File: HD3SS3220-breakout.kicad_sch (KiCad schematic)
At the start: 36 parts, among them J2 USB_C_Receptacle, SW2 SW_DIP_x04, U4 HD3SS3220RNHR, U5 U-A-39SS-Y-1, U6 HT7533-1_C14289, U7 TPD4EUSB30, U8 TPD2EUSB30, U9 PZ254-2-08-WS

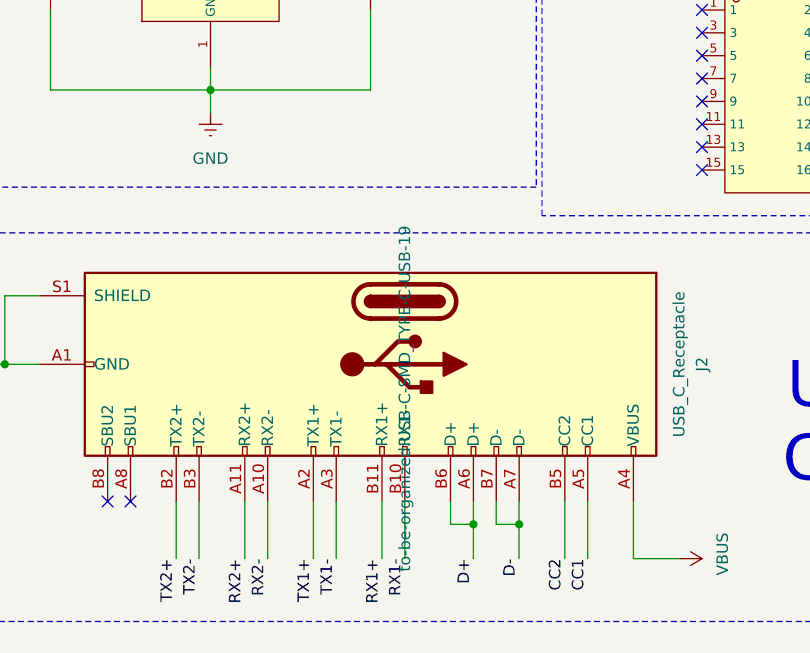
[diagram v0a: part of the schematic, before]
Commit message: Added dip switch footprint to library and PCB editor
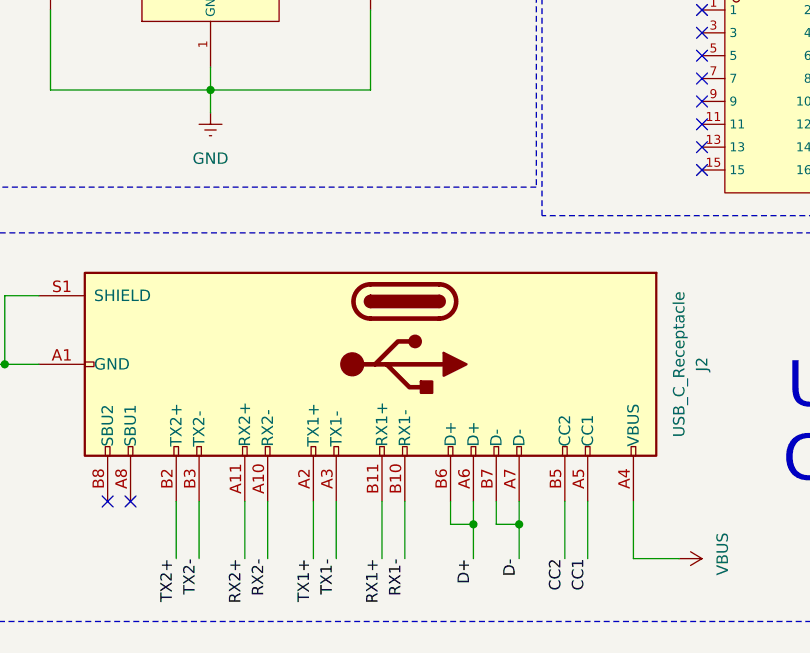
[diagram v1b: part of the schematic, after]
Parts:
- SW2: footprint (none) -> Button_Switch_SMD:SW4
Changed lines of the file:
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@@
 		(property "Footprint" "to-be-organized:USB-C-SMD_TYPE-C-USB-19"
 			(at 68.58 171.45 0)
+			(hide yes)
 			(show_name no)
 			(do_not_autoplace no)
@@
 			)
 		)
-		(property "Footprint" ""
+		(property "Footprint" "Button_Switch_SMD:SW4"
 			(at 204.47 146.05 0)
 			(hide yes)

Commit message: added more footprints
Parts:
- C1, C11, C12, C2, C3, C4, C5, C6: footprint (none) -> Capacitor_SMD:C_0603_1608Metric
- DIR_LED1, VBUS_LED1: footprint (none) -> LED_SMD:LED_0603_1608Metric
- R10, R6, R7, R8, R9: footprint (none) -> Resistor_SMD:R_0603_1608Metric
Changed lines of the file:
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@@
 (kicad_sch
-	(version 20260306)
+	(version 20260101)
 	(generator "eeschema")
 	(generator_version "10.0")
@@
 			)
 		)
-		(property "Footprint" ""
+		(property "Footprint" "Resistor_SMD:R_0603_1608Metric"
 			(at 175.26 49.53 0)
 			(hide yes)
@@
 			)
 		)
-		(property "Footprint" ""
+		(property "Footprint" "Capacitor_SMD:C_0603_1608Metric"
 			(at 247.65 52.07 0)
 			(hide yes)
@@
 			)
 		)
-		(property "Footprint" ""
+		(property "Footprint" "LED_SMD:LED_0603_1608Metric"
 			(at 154.94 92.71 0)
 			(hide yes)
@@
 			)
 		)
-		(property "Footprint" ""
+		(property "Footprint" "Resistor_SMD:R_0603_1608Metric"
 			(at 189.23 143.51 0)
 			(hide yes)
@@
 			)
 		)
-		(property "Footprint" ""
+		(property "Footprint" "Capacitor_SMD:C_0603_1608Metric"
 			(at 255.27 67.31 0)
 			(hide yes)
@@
 			)
 		)
-		(property "Footprint" ""
+		(property "Footprint" "Resistor_SMD:R_0603_1608Metric"
 			(at 217.17 146.05 0)
 			(hide yes)
@@
 			)
 		)
-		(property "Footprint" ""
+		(property "Footprint" "Resistor_SMD:R_0603_1608Metric"
 			(at 217.17 148.59 0)
 			(hide yes)
@@
 			)
 		)
-		(property "Footprint" ""
+		(property "Footprint" "Capacitor_SMD:C_0603_1608Metric"
 			(at 247.65 64.77 0)
 			(hide yes)
@@
 			)
 		)
-		(property "Footprint" ""
+		(property "Footprint" "Capacitor_SMD:C_0603_1608Metric"
 			(at 64.77 125.73 0)
 			(hide yes)
@@
 			)
 		)
-		(property "Footprint" ""
+		(property "Footprint" "LED_SMD:LED_0603_1608Metric"
 			(at 144.78 92.71 0)
 			(hide yes)
@@
 			)
 		)
-		(property "Footprint" ""
+		(property "Footprint" "Capacitor_SMD:C_0603_1608Metric"
 			(at 171.45 77.47 0)
 			(hide yes)
@@
 			)
 		)
-		(property "Footprint" ""
+		(property "Footprint" "Capacitor_SMD:C_0603_1608Metric"
 			(at 29.21 125.73 0)
 			(hide yes)
@@
 			)
 		)
-		(property "Footprint" ""
+		(property "Footprint" "Resistor_SMD:R_0603_1608Metric"
 			(at 166.37 41.91 0)
 			(hide yes)
@@
 			)
 		)
-		(property "Footprint" ""
+		(property "Footprint" "Capacitor_SMD:C_0603_1608Metric"
 			(at 176.53 80.01 0)
 			(hide yes)
@@
 			)
 		)
-		(property "Footprint" ""
+		(property "Footprint" "Capacitor_SMD:C_0603_1608Metric"
 			(at 255.27 54.61 0)
 			(hide yes)

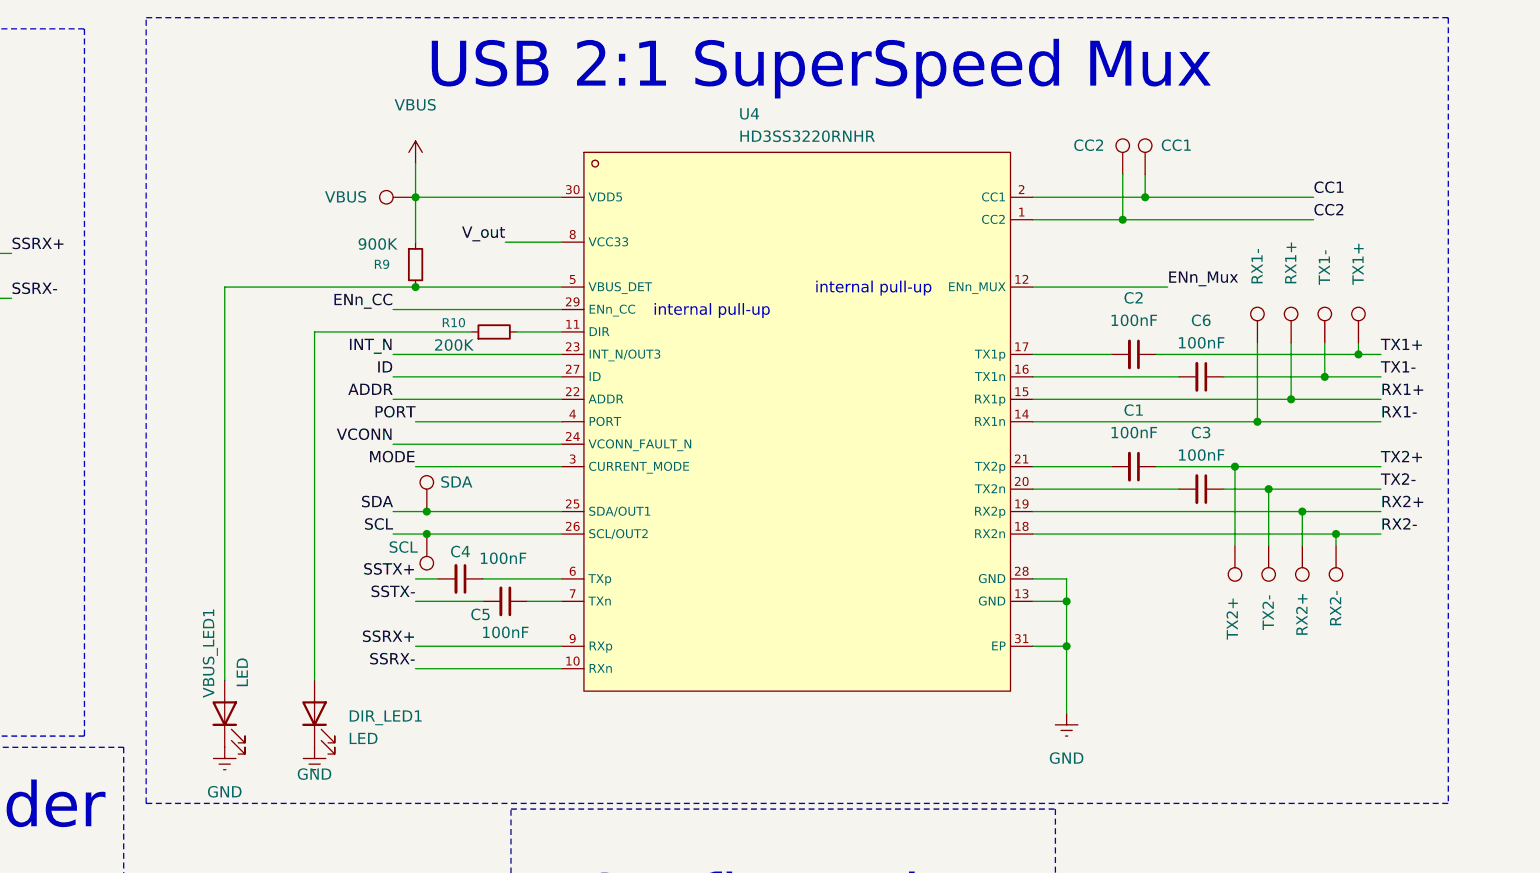
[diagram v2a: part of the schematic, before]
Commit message: Fixed mux footprint somewhat, starting to route
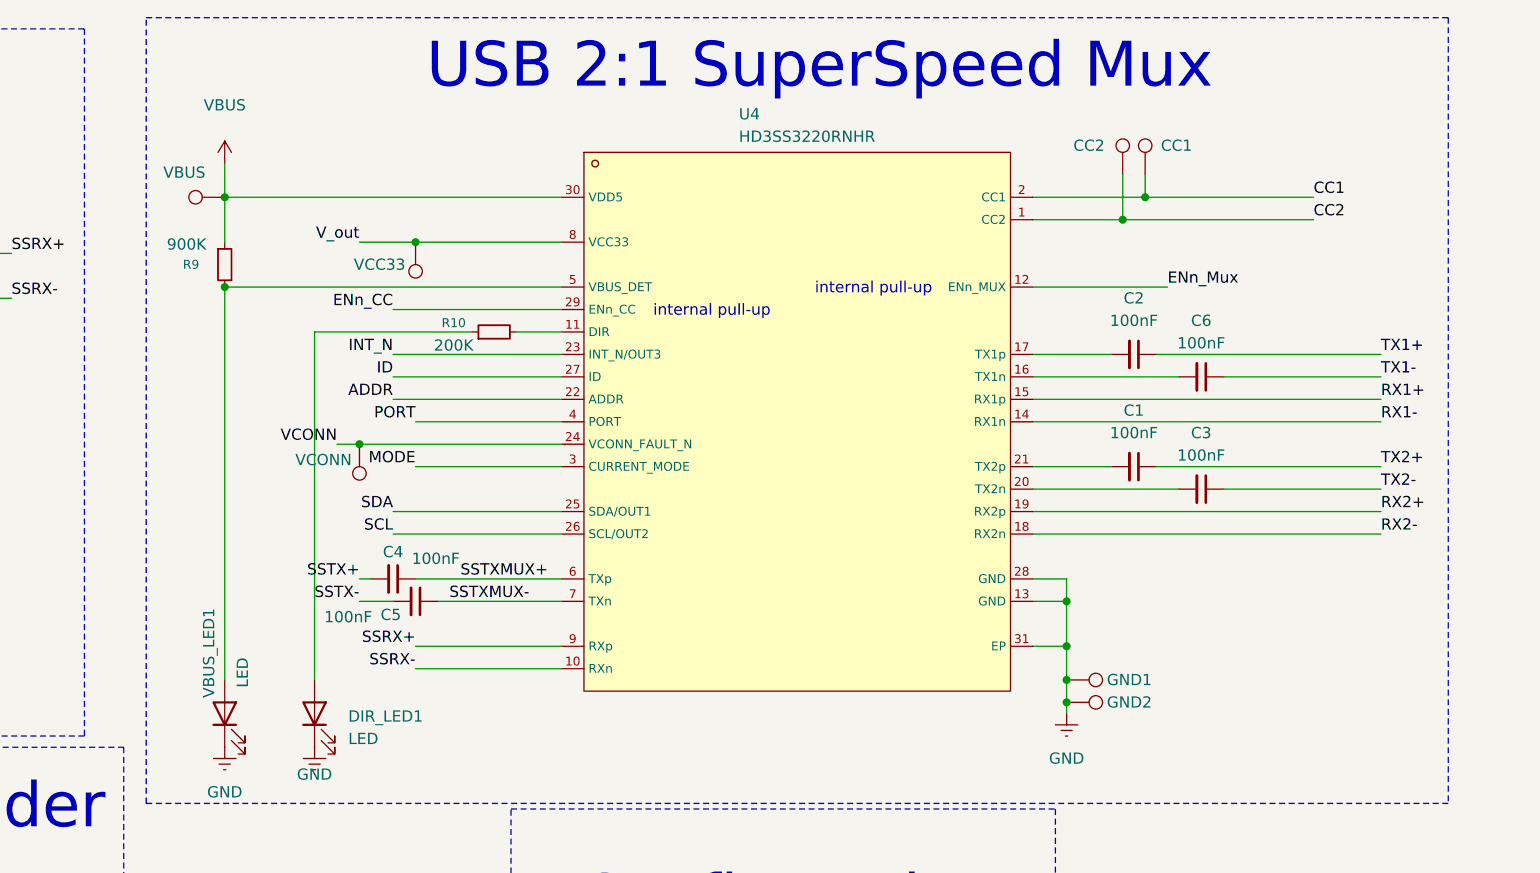
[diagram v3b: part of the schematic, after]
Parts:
- removed TP1: RX2-, symbol Connector:TestPoint
- removed TP2: RX1-, symbol Connector:TestPoint
- removed TP3: RX2+, symbol Connector:TestPoint
- removed TP4: TX2-, symbol Connector:TestPoint
- removed TP5: TX2+, symbol Connector:TestPoint
- removed TP6: RX1+, symbol Connector:TestPoint
- removed TP7: TX1-, symbol Connector:TestPoint
- removed TP8: TX1+, symbol Connector:TestPoint
- added TP14: GND1, TestPoint:TestPoint_Keystone_5000-5004_Miniature, symbol Connector:TestPoint
- added TP15: GND2, TestPoint:TestPoint_Keystone_5000-5004_Miniature, symbol Connector:TestPoint
- TP10, TP11, TP9: footprint (none) -> TestPoint:TestPoint_Pad_D1.5mm
- TP12: value SDA -> VCC33; footprint (none) -> TestPoint:TestPoint_Pad_D1.5mm
- TP13: value SCL -> VCONN; footprint (none) -> TestPoint:TestPoint_Pad_D1.5mm
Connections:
- net GND: now also TP14.1, TP15.1
- net SCL: no longer TP13.1
- net SDA: no longer TP12.1
- net VCONN: now also TP13.1
- net V_out: now also TP12.1
- net SSTXMUX+: now reaches C4.1, U4.6 (TXp)
- net SSTXMUX-: now reaches C5.1, U4.7 (TXn)
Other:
- moved on the sheet: C4, C5, R9

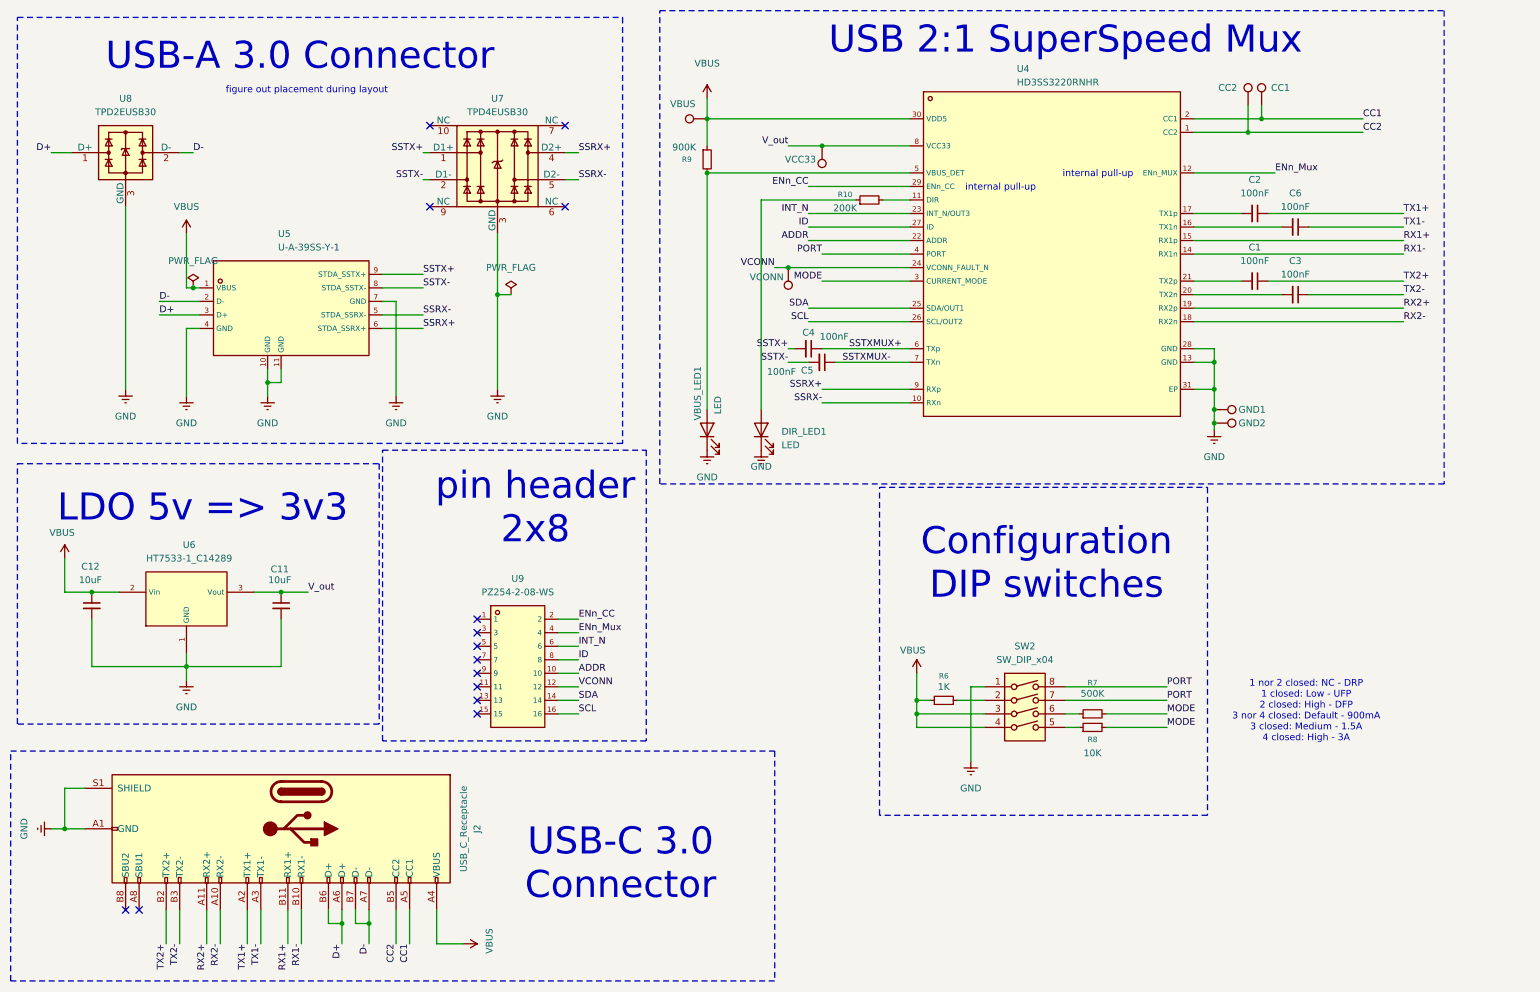
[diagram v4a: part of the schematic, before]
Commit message: Hierarchy Schematic Implementation and Clean-up (Please Refer to this Version for previous sym-lib-table)
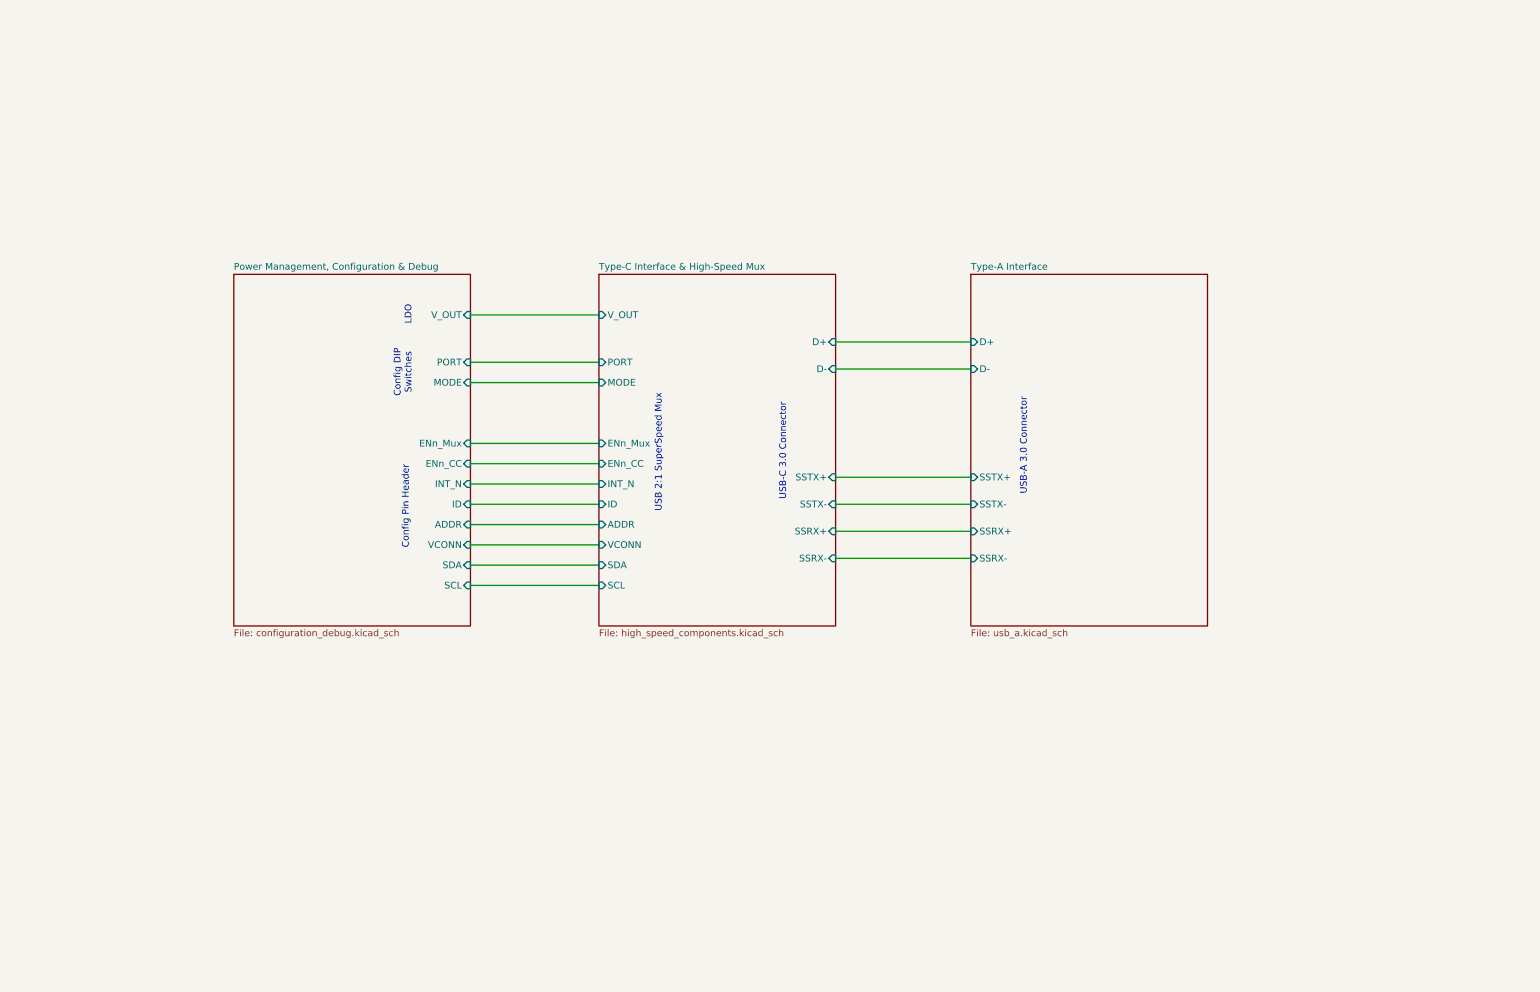
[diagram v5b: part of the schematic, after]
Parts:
- removed C1, C2, C3, C4, C5, C6: 100nF, Capacitor_SMD:C_0603_1608Metric, symbol Device:C_Small
- removed C11, C12: 10uF, Capacitor_SMD:C_0603_1608Metric, symbol Device:C_Small
- removed DIR_LED1, VBUS_LED1: LED, LED_SMD:LED_0603_1608Metric, symbol Device:LED
- removed J2: USB_C_Receptacle, to-be-organized:USB-C-SMD_TYPE-C-USB-19, symbol Connector:USB_C_Receptacle
- removed R10: 200K, Resistor_SMD:R_0603_1608Metric, symbol Device:R_Small
- removed R6: 1K, Resistor_SMD:R_0603_1608Metric, symbol Device:R_Small
- removed R7: 500K, Resistor_SMD:R_0603_1608Metric, symbol Device:R_Small
- removed R8: 10K, Resistor_SMD:R_0603_1608Metric, symbol Device:R_Small
- removed R9: 900K, Resistor_SMD:R_0603_1608Metric, symbol Device:R_Small
- removed SW2: SW_DIP_x04, Button_Switch_SMD:SW4, symbol Switch:SW_DIP_x04
- removed TP10: CC2, TestPoint:TestPoint_Pad_D1.5mm, symbol Connector:TestPoint
- removed TP11: VBUS, TestPoint:TestPoint_Pad_D1.5mm, symbol Connector:TestPoint
- removed TP12: VCC33, TestPoint:TestPoint_Pad_D1.5mm, symbol Connector:TestPoint
- removed TP13: VCONN, TestPoint:TestPoint_Pad_D1.5mm, symbol Connector:TestPoint
- removed TP14: GND1, TestPoint:TestPoint_Keystone_5000-5004_Miniature, symbol Connector:TestPoint
- removed TP15: GND2, TestPoint:TestPoint_Keystone_5000-5004_Miniature, symbol Connector:TestPoint
- removed TP9: CC1, TestPoint:TestPoint_Pad_D1.5mm, symbol Connector:TestPoint
- removed U4: HD3SS3220RNHR, Interface_USB:HD3SS3220IRNHR, symbol Interface_USB:HD3SS3220RNHR
- removed U5: U-A-39SS-Y-1, footprint:USB-3.0-A_U-A-39SS-Y-1, symbol Connector_USB-custom:U-A-39SS-Y-1
- removed U6: HT7533-1_C14289, footprint:SOT-89-3_L4.5-W2.5-P1.50-LS4.2-BR, symbol Regulator_Linear:HT7533-1_C14289
- removed U7: TPD4EUSB30, Package_SON:USON-10_2.5x1.0mm_P0.5mm, symbol Power_Protection:TPD4EUSB30
- removed U8: TPD2EUSB30, Package_TO_SOT_SMD:Texas_DRT-3, symbol Power_Protection:TPD2EUSB30
- removed U9: PZ254-2-08-WS, footprint:HDR-SMD_16P-P2.54-H-M-R2-C8-W12.0-N, symbol PZ254-2-08-WS:PZ254-2-08-WS
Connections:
- no-connect marks 14 -> 0
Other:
- added sheet Power Management, Configuration & Debug (configuration_debug.kicad_sch)
- added sheet Type-A Interface (usb_a.kicad_sch)
- added sheet Type-C Interface & High-Speed Mux (high_speed_components.kicad_sch)
- note added: "Config DIP Switches"
- note added: "Config Pin Header"
- note added: "LDO"
- note removed: "1 nor 2 closed: NC - DRP 1 closed: Low - UFP 2 closed: High - DFP 3 nor 4 closed: Default - 900mA 3 closed: Medium - 1.5A 4 closed: High - 3A"
- note removed: "Configuration DIP switches"
- note removed: "LDO 5v => 3v3"
- note removed: "figure out placement during layout"
- note removed: "internal pull-up"
- note removed: "pin header 2x8"
- company: (none) -> UWaterloo Reality Labs
- title: (none) -> USB-3.0 Bridging Board Root
